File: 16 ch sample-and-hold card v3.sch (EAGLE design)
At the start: 32 parts, among them IC2 TL074D, IC3 TL074D, IC4 TL074D, IC5 TL074D, IC6 DG408DY, IC7 DG408DY

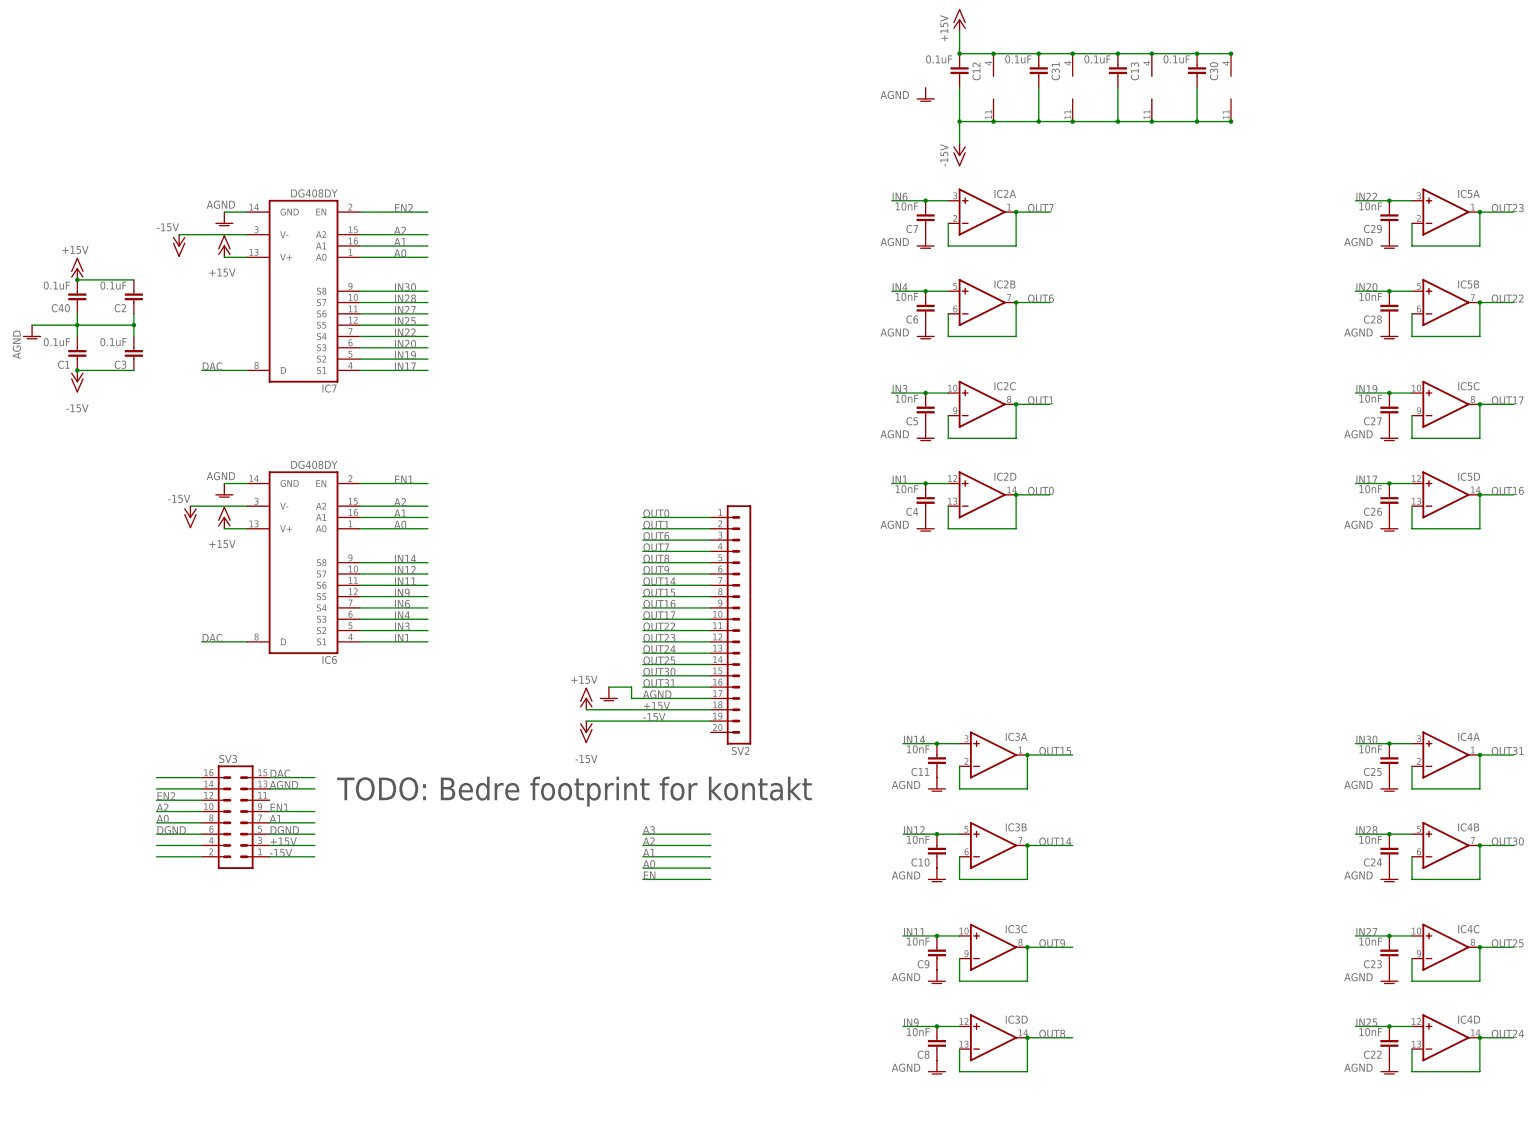
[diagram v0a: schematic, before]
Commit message: Completed silk etc
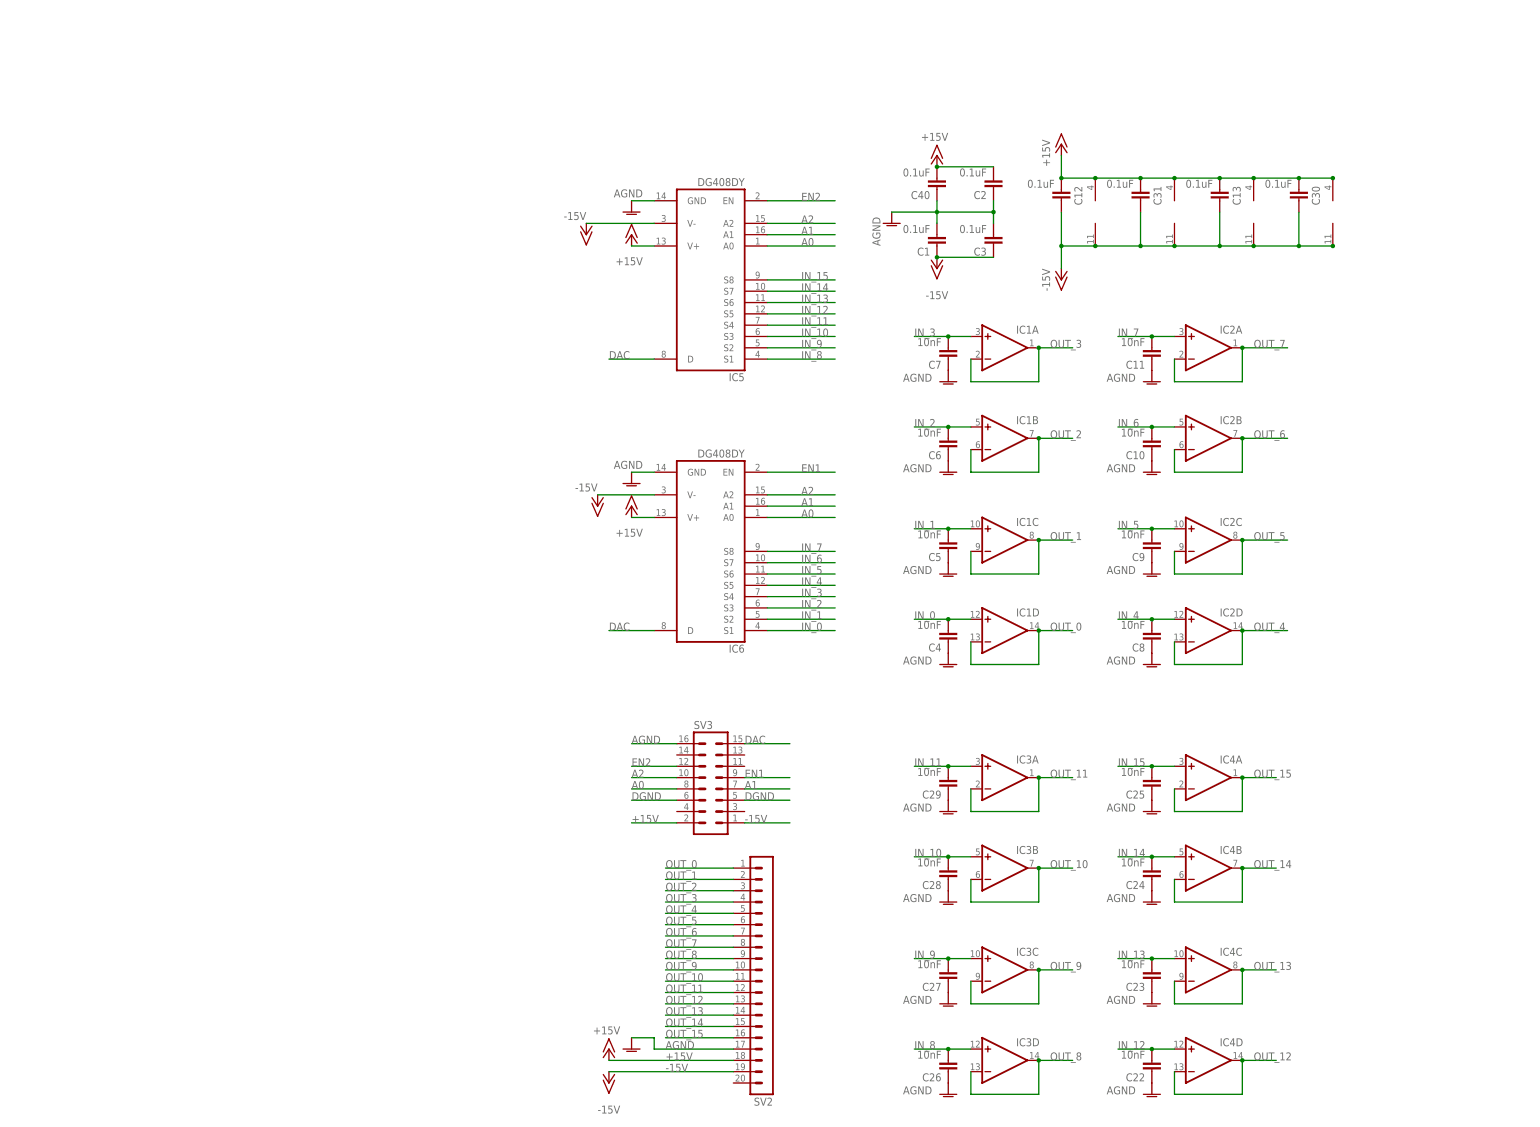
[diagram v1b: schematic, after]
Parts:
- removed IC7: DG408DY, maxim:DG408DY
- added IC1: TL074D, linear:TL074D
- IC5: value TL074D -> DG408DY; device linear:TL074D -> maxim:DG408DY
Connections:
- net OUT24 renamed OUT_12
- net OUT25 renamed OUT_13
- net OUT30 renamed OUT_14
- net OUT31 renamed OUT_15
- removed net IN1: C4.2, IC2D.+IN, IC6.S1
- removed net IN11: C9.2, IC3C.+IN, IC6.S6
- removed net IN12: C10.2, IC3B.+IN, IC6.S7
- removed net IN14: C11.2, IC3A.+IN, IC6.S8
- removed net IN17: C26.2, IC5D.+IN, IC7.S1
- removed net IN19: C27.2, IC5C.+IN, IC7.S2
- removed net IN20: C28.2, IC5B.+IN, IC7.S3
- removed net IN22: C29.2, IC5A.+IN, IC7.S4
- removed net IN25: C22.2, IC4D.+IN, IC7.S5
- removed net IN27: C23.2, IC4C.+IN, IC7.S6
- removed net IN28: C24.2, IC4B.+IN, IC7.S7
- removed net IN3: C5.2, IC2C.+IN, IC6.S2
- removed net IN30: C25.2, IC4A.+IN, IC7.S8
- removed net IN4: C6.2, IC2B.+IN, IC6.S3
- removed net IN6: C7.2, IC2A.+IN, IC6.S4
- removed net IN9: C8.2, IC3D.+IN, IC6.S5
- removed net N$1: SV3.16
- removed net N$15: SV3.4
- removed net N$16: SV3.2
- removed net N$3: SV3.14
- removed net OUT0: IC2D.-IN, IC2D.OUT, SV2.1
- removed net OUT1: IC2C.-IN, IC2C.OUT, SV2.2
- removed net OUT14: IC3B.-IN, IC3B.OUT, SV2.7
- removed net OUT15: IC3A.-IN, IC3A.OUT, SV2.8
- removed net OUT16: IC5D.-IN, IC5D.OUT, SV2.9
- removed net OUT17: IC5C.-IN, IC5C.OUT, SV2.10
- removed net OUT22: IC5B.-IN, IC5B.OUT, SV2.11
- removed net OUT23: IC5A.-IN, IC5A.OUT, SV2.12
- removed net OUT6: IC2B.-IN, IC2B.OUT, SV2.3
- removed net OUT7: IC2A.-IN, IC2A.OUT, SV2.4
- removed net OUT8: IC3D.-IN, IC3D.OUT, SV2.5
- removed net OUT9: IC3C.-IN, IC3C.OUT, SV2.6
- new net IN_0: C4.2, IC1D.+IN, IC6.S1
- new net IN_1: C5.2, IC1C.+IN, IC6.S2
- new net IN_10: C28.2, IC3B.+IN, IC5.S3
- new net IN_11: C29.2, IC3A.+IN, IC5.S4
- new net IN_12: C22.2, IC4D.+IN, IC5.S5
- new net IN_13: C23.2, IC4C.+IN, IC5.S6
- new net IN_14: C24.2, IC4B.+IN, IC5.S7
- new net IN_15: C25.2, IC4A.+IN, IC5.S8
- new net IN_2: C6.2, IC1B.+IN, IC6.S3
- new net IN_3: C7.2, IC1A.+IN, IC6.S4
- new net IN_4: C8.2, IC2D.+IN, IC6.S5
- new net IN_5: C9.2, IC2C.+IN, IC6.S6
- new net IN_6: C10.2, IC2B.+IN, IC6.S7
- new net IN_7: C11.2, IC2A.+IN, IC6.S8
- new net IN_8: C26.2, IC3D.+IN, IC5.S1
- new net IN_9: C27.2, IC3C.+IN, IC5.S2
- new net OUT_0: IC1D.-IN, IC1D.OUT, SV2.1
- new net OUT_1: IC1C.-IN, IC1C.OUT, SV2.2
- new net OUT_10: IC3B.-IN, IC3B.OUT, SV2.11
- new net OUT_11: IC3A.-IN, IC3A.OUT, SV2.12
- new net OUT_2: IC1B.-IN, IC1B.OUT, SV2.3
- new net OUT_3: IC1A.-IN, IC1A.OUT, SV2.4
- new net OUT_4: IC2D.-IN, IC2D.OUT, SV2.5
- new net OUT_5: IC2C.-IN, IC2C.OUT, SV2.6
- new net OUT_6: IC2B.-IN, IC2B.OUT, SV2.7
- new net OUT_7: IC2A.-IN, IC2A.OUT, SV2.8
- new net OUT_8: IC3D.-IN, IC3D.OUT, SV2.9
- new net OUT_9: IC3C.-IN, IC3C.OUT, SV2.10
- net +15V: now also IC1P.V+, IC5.V+, SV3.2; no longer IC5P.V+, IC7.V+, SV3.3
- net -15V: now also IC1P.V-, IC5.V-; no longer IC5P.V-, IC7.V-
- net A0: now also IC5.A0; no longer IC7.A0
- net A1: now also IC5.A1; no longer IC7.A1
- net A2: now also IC5.A2; no longer IC7.A2
- net AGND: now also IC5.GND, SV3.16; no longer IC7.GND, SV3.13
- net DAC: now also IC5.D; no longer IC7.D
- net EN2: now also IC5.EN; no longer IC7.EN
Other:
- note removed: "TODO: Bedre footprint for kontakt"
- moved on the sheet: C1, C10, C11, C12, C13, C2, C22, C23, C24, C25, C26, C27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
